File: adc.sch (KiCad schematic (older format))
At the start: 43 parts

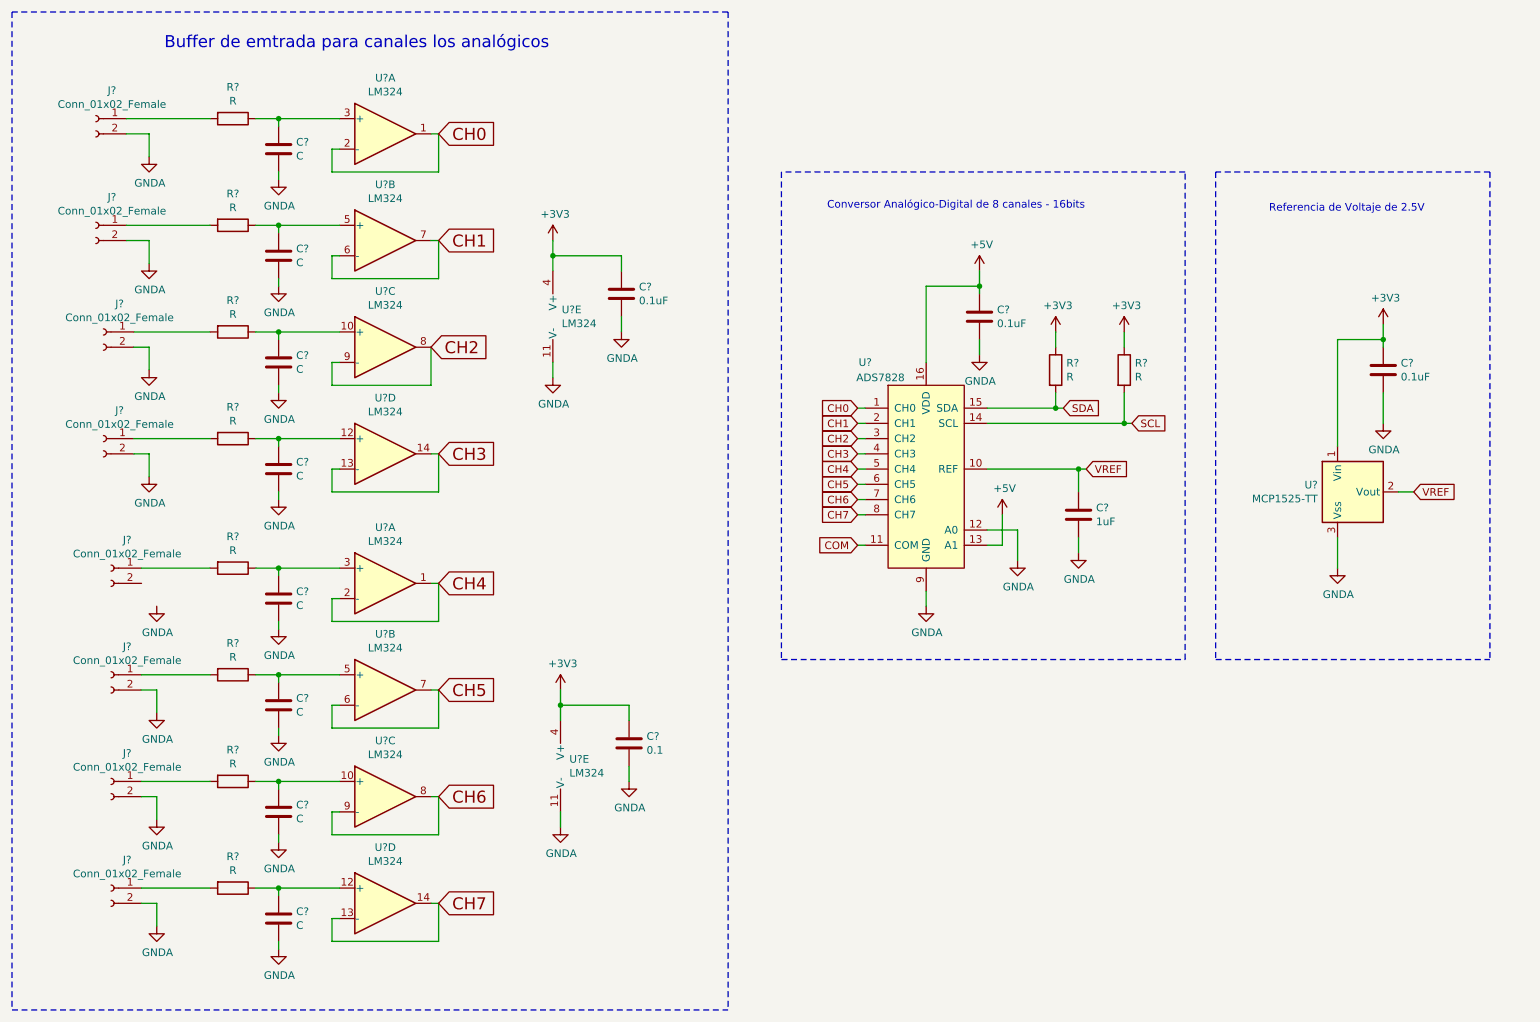
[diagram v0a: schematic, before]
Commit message: Se hace cambios en el esquematico y se anexa PCB
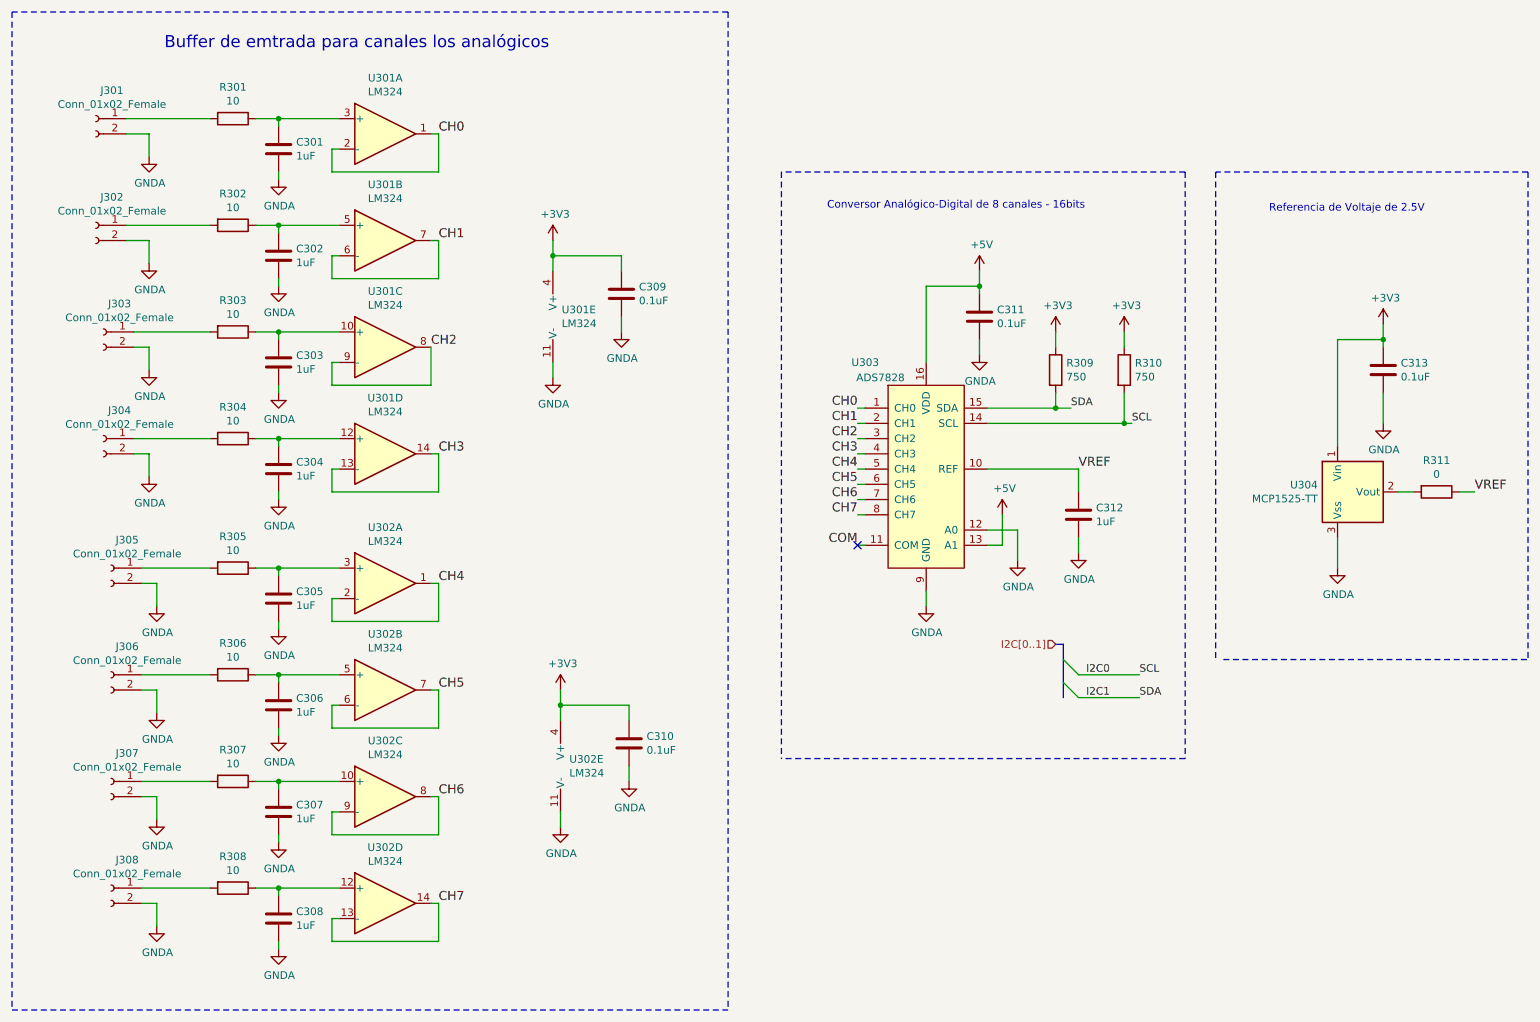
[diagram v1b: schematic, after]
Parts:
- added R311: 0, Resistor_SMD:R_0805_2012Metric_Pad1.15x1.40mm_HandSolder, symbol Device:R
- C301, C302, C303, C304, C305, C306, C307, C308: renamed from C?; value C -> 1uF; footprint (none) -> Capacitor_SMD:C_0805_2012Metric_Pad1.15x1.40mm_HandSolder
- C309, C311, C312, C313: renamed from C?; footprint (none) -> Capacitor_SMD:C_0805_2012Metric_Pad1.15x1.40mm_HandSolder
- C310: renamed from C?; value 0.1 -> 0.1uF; footprint (none) -> Capacitor_SMD:C_0805_2012Metric_Pad1.15x1.40mm_HandSolder
- J301, J302, J303, J304, J305, J306, J307, J308: renamed from J?; footprint (none) -> Connector_PinHeader_1.27mm:PinHeader_1x02_P1.27mm_Vertical
- R301, R302, R303, R304, R305, R306, R307, R308: renamed from R?; value R -> 10; footprint (none) -> Resistor_SMD:R_0805_2012Metric_Pad1.15x1.40mm_HandSolder
- R309, R310: renamed from R?; value R -> 750; footprint (none) -> Resistor_SMD:R_0805_2012Metric_Pad1.15x1.40mm_HandSolder
- U301, U302: renamed from U?; footprint (none) -> Package_SO:SOIC-14_3.9x8.7mm_P1.27mm
- gave numbers to parts that had none: 2
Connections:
- net GNDA: now also J305.2 (Pin_2)
- net VREF: now also R311.1; no longer U304.2 (Vout)
- net SCL renamed I2C0
- net SDA renamed I2C1
- new net: R311.2, U304.2 (Vout)
- no-connect marks 0 -> 1

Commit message: Se realizan correcciones finales y se agregan carpetas BOM, Datasheet, Doc, Gerbers, lib.pretty y shapes3D
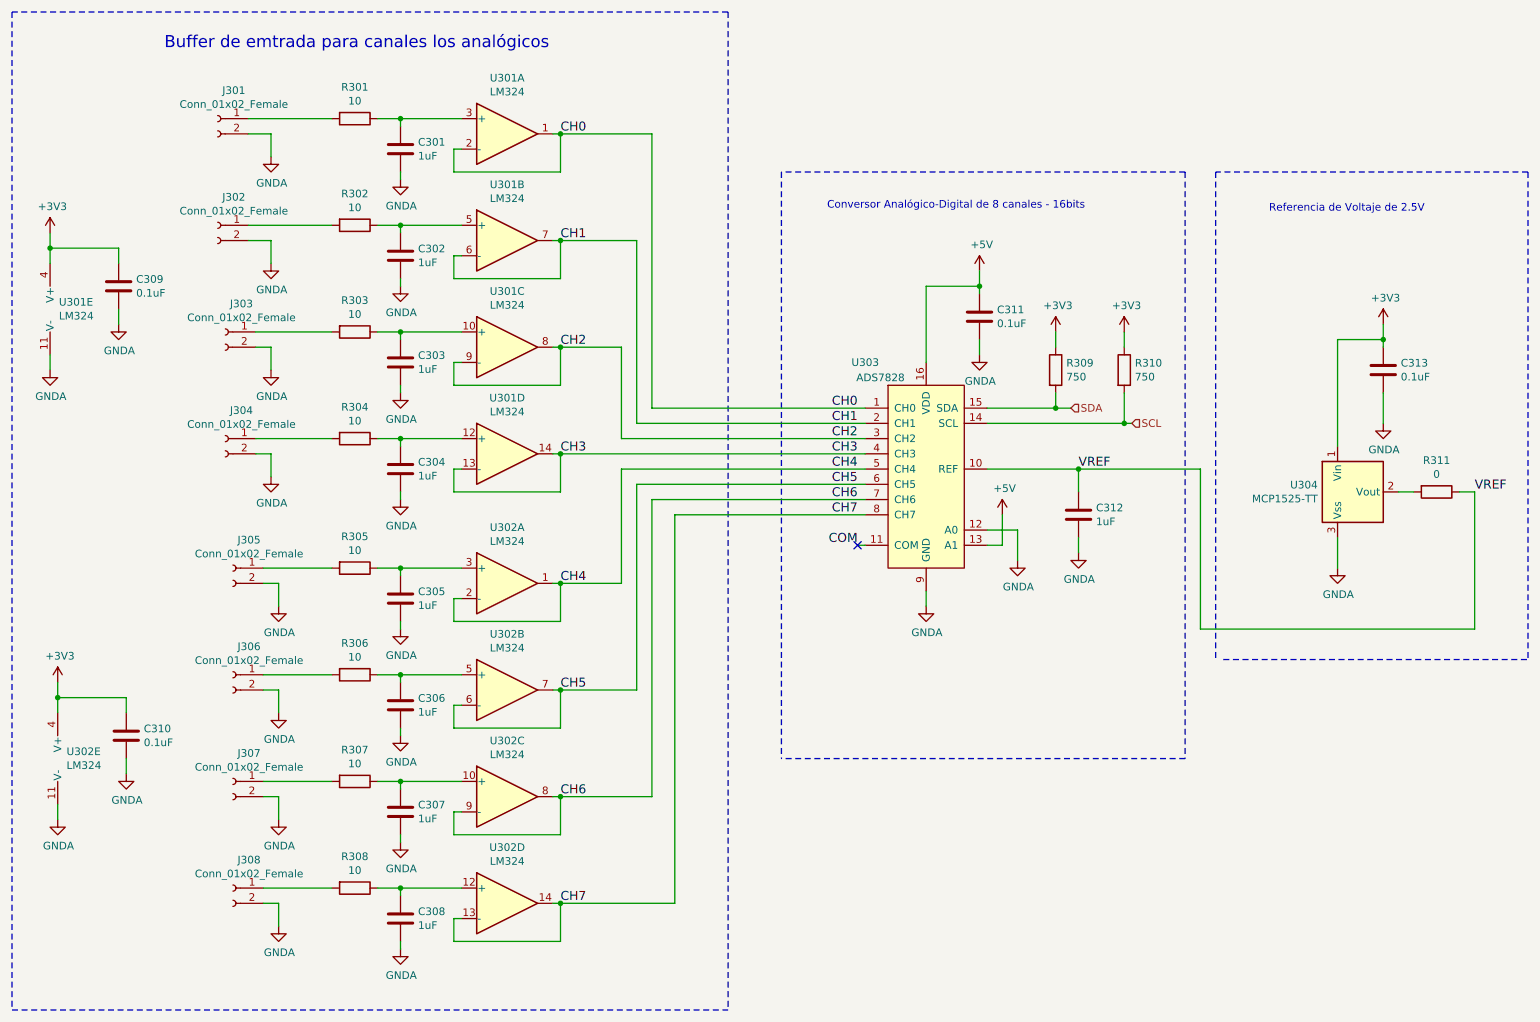
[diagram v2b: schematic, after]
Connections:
- net I2C0 renamed SCL
- net I2C1 renamed SDA
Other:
- moved on the sheet: C301, C302, C303, C304, C305, C306, C307, C308, C309, C310, J301, J302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
